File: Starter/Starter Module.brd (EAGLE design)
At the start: 25.4 x 25.4 mm, 3 parts

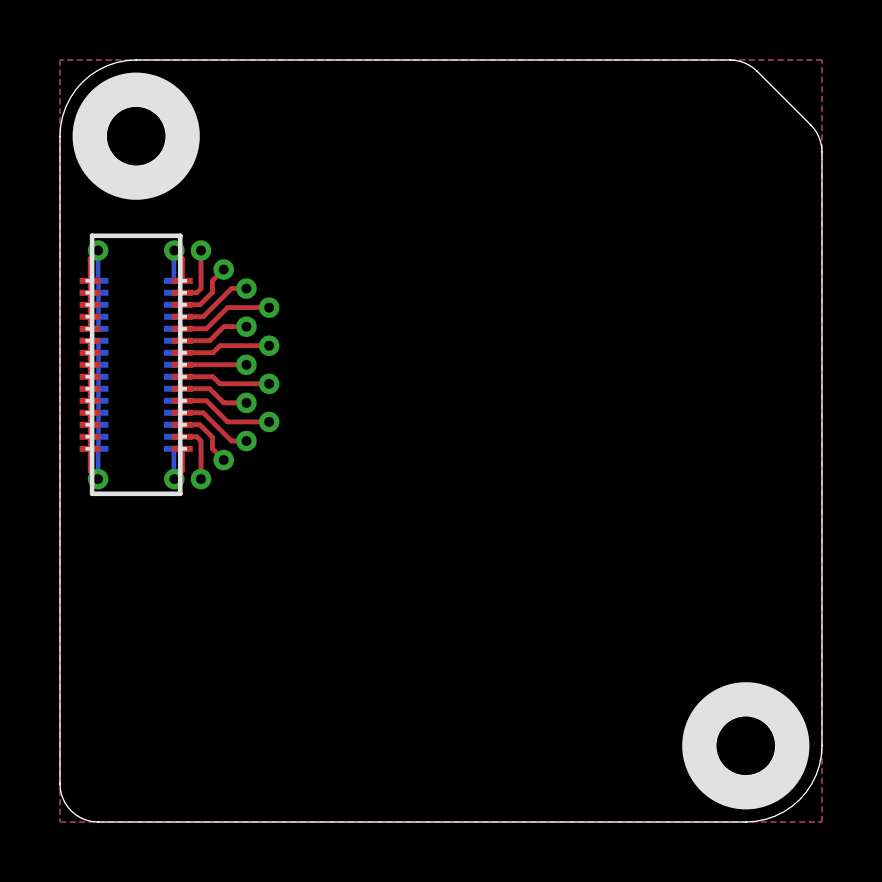
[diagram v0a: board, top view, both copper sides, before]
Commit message: Updated Starter Module with standard silkscreen and included all libraries.
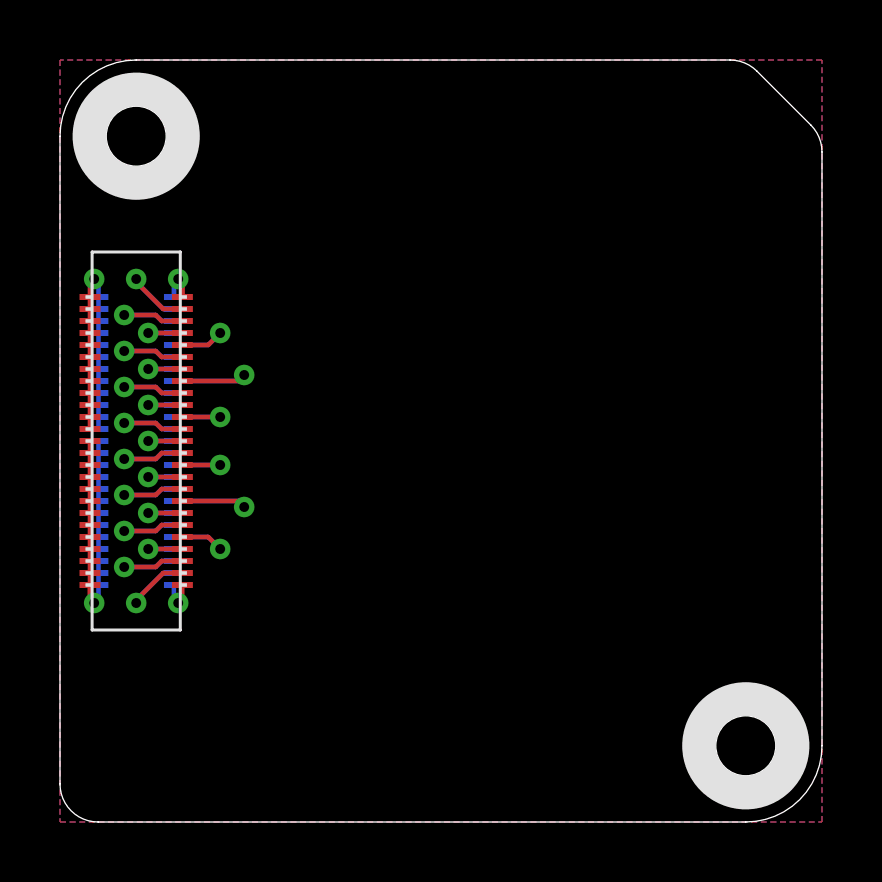
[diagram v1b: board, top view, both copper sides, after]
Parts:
- renumbered U$8 to U$2
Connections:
- new net N$18: U$2.TDI, U$2.TDI@1, U$2.TDI@VIA
- new net N$19: U$2.TDO, U$2.TDO@1, U$2.TDO@VIA
- new net N$20: U$2.TCK, U$2.TCK@1, U$2.TCK@VIA
- new net N$21: U$2.TMS, U$2.TMS@1, U$2.TMS@VIA
- new net N$22: U$2.TRST, U$2.TRST@1, U$2.TRST@VIA
- new net N$23: U$2.RXI.DBG, U$2.RXI.DBG@1, U$2.RXI.DBG@VIA
- new net N$24: U$2.TXO.DBG, U$2.TXO.DBG@1, U$2.TXO.DBG@VIA
- new net N$25: U$2.RST, U$2.RST@1, U$2.RST@VIA
- new net N$8: U$2.TXO, U$2.TXO@1, U$2.TXO@VIA
- new net N$9: U$2.RXI, U$2.RXI@1, U$2.RXI@VIA
- net 3.3V: now also U$2.3.3V@11, U$2.3.3V@12, U$2.3.3V@13, U$2.3.3V@14, U$2.3.3V@15, U$2.3.3V@16, U$2.3.3V@17, U$2.3.3V@18, U$2.3.3V@19, U$2.3.3V@20, U$2.3.3V@21, U$2.3.3V@22, U$2.3.3V@23, U$2.3.3V@24
- net GND: now also U$2.GND@21, U$2.GND@22, U$2.GND@23, U$2.GND@24, U$2.GND@25, U$2.GND@26
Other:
- board text added: "Cruz Monrreal II"
- board text added: "InnovativeMaker.com"
- board text added: "v1"
